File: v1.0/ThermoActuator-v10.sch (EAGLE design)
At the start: 58 parts, among them IC1 LM358D, IC2 ULN2003AD, IC3 LM358D

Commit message: all channels laid out
somewhat inconsistent but all elements
laid out except the button
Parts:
- added C5, C6, C7, C8: 10nF, rcl:C-EUC1206
- added IC4, IC5: LM358D, linear:LM358D
- added JP1: (no value), SparkFun:M06LOCK
- added JP24, JP25, JP26: M022.54MM_SCREWTERM, SparkFun-Connectors:M022.54MM_SCREWTERM
- added R19, R20, R21, R22: 100K, rcl:R-EU_R0805
- added R23, R24, R25, R26: 10K, rcl:R-EU_R1206
- IC1: value LM358D -> ULN2003AD; device linear:LM358D -> uln-udn:ULN2003AD
- IC2: value ULN2003AD -> LM358D; device uln-udn:ULN2003AD -> linear:LM358D
- JP10: value (none) -> M022.54MM_SCREWTERM; device SparkFun:M06LOCK -> SparkFun-Connectors:M022.54MM_SCREWTERM
- JP11, JP12: value (none) -> M022.54MM_SCREWTERM; device SparkFun:M02LOCK -> SparkFun-Connectors:M022.54MM_SCREWTERM
- JP13, JP19, JP20, JP21, JP22, JP23: value ADC2 -> M022.54MM_SCREWTERM
- JP14: value OUT1 -> M022.54MM_SCREWTERM
- JP15: value OUT2 -> (none); device SparkFun-Connectors:M022.54MM_SCREWTERM -> SparkFun:M02LOCK
- JP16, JP17: value ADC2 -> M16LOCK; device SparkFun-Connectors:M022.54MM_SCREWTERM -> SparkFun:M16LOCK
- JP18: value ADC2 -> (none); device SparkFun-Connectors:M022.54MM_SCREWTERM -> SparkFun:M02LOCK
- JP2: value ADC1 -> (none); device SparkFun-Connectors:M022.54MM_SCREWTERM -> SparkFun:M08LOCK
- JP7: value (none) -> M022.54MM_SCREWTERM; device SparkFun:M08LOCK -> SparkFun-Connectors:M022.54MM_SCREWTERM
- JP8, JP9: value M16LOCK -> M022.54MM_SCREWTERM; device SparkFun:M16LOCK -> SparkFun-Connectors:M022.54MM_SCREWTERM
- R1: value 330 -> (none)
- R11, R12, R13, R14: value 330 -> 100K
- R15, R17: value 100K -> 10K; device rcl:R-EU_R0805 -> rcl:R-EU_R1206
- R3: value (none) -> 330
- R4, R6: value 100K -> 330
- R5, R7: value 10K -> 330; device rcl:R-EU_R1206 -> rcl:R-EU_R0805
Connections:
- new net AS4: IC4A.-IN, IC4A.OUT, SW1.12
- new net AS5: IC4B.-IN, IC4B.OUT, SW1.11
- new net AS6: IC5A.-IN, IC5A.OUT, SW1.10
- new net AS7: IC5B.-IN, IC5B.OUT, SW1.9
- new net N$24: JP23.2, R19.1, R23.1
- new net N$25: C5.2, IC4A.+IN, R23.2
- new net N$26: JP24.2, R20.1, R24.1
- new net N$27: C6.2, IC4B.+IN, R24.2
- new net N$28: JP25.2, R21.1, R25.1
- new net N$29: C7.2, IC5A.+IN, R25.2
- new net N$30: JP26.2, R22.1, R26.1
- new net N$31: C8.2, IC5B.+IN, R26.2
- net 3.3: now also JP1.2; no longer JP10.2
- net 5V: now also JP1.3, R2.2; no longer JP10.3, R3.2
- net A10: now also IC1.I3; no longer IC2.I3
- net A11: now also IC1.I4; no longer IC2.I4
- net A12: now also IC1.I5; no longer IC2.I5
- net A13: now also IC1.I6; no longer IC2.I6
- net A14: now also IC1.I7; no longer IC2.I7
- net A8: now also IC1.I1; no longer IC2.I1
- net A9: now also IC1.I2; no longer IC2.I2
- net AO0: now also IC1.O1, JP7.2; no longer IC2.O1, JP14.2
- net AO1: now also IC1.O2, JP8.2; no longer IC2.O2, JP15.2
- net AO2: now also IC1.O3, JP9.2; no longer IC2.O3, JP16.2
- net AO3: now also IC1.O4, JP10.2; no longer IC2.O4, JP17.2
- net AO4: now also IC1.O5, JP11.2; no longer IC2.O5, JP18.2
- net AO5: now also IC1.O6, JP12.2; no longer IC2.O6, JP19.2
- net AO6: now also IC1.O7, JP13.2; no longer IC2.O7, JP20.2
- net AO7: now also JP14.2; no longer JP21.2
- net AREF: now also JP2.8; no longer JP3.8
- net AS0: now also IC2A.-IN, IC2A.OUT; no longer IC1A.-IN, IC1A.OUT
- net AS1: now also IC2B.-IN, IC2B.OUT; no longer IC1B.-IN, IC1B.OUT
- net D10: now also JP2.3; no longer JP3.3
- net D11: now also JP2.4; no longer JP3.4
- net D12: now also JP2.5; no longer JP3.5
- net D13: now also JP2.6, R3.2; no longer JP3.6, R2.2
- net D22: now also JP17.1; no longer JP9.1
- net D23: now also JP16.16; no longer JP8.16
- net D24: now also JP17.2; no longer JP9.2
- net D25: now also JP16.15; no longer JP8.15
- net D26: now also JP17.3; no longer JP9.3
- net D27: now also JP16.14; no longer JP8.14
- net D28: now also JP17.4; no longer JP9.4
- net D29: now also JP16.13; no longer JP8.13
- net D30: now also JP17.5; no longer JP9.5
- net D31: now also JP16.12; no longer JP8.12
- net D32: now also JP17.6; no longer JP9.6
- net D33: now also JP16.11; no longer JP8.11
- net D34: now also JP17.7; no longer JP9.7
- net D35: now also JP16.10; no longer JP8.10
- net D36: now also JP17.8; no longer JP9.8
- net D37: now also JP16.9; no longer JP8.9
- net D38: now also JP17.9; no longer JP9.9
- net D39: now also JP16.8; no longer JP8.8
- net D40: now also JP17.10; no longer JP9.10
- net D41: now also JP16.7; no longer JP8.7
- net D42: now also JP17.11; no longer JP9.11
- net D43: now also JP16.6; no longer JP8.6
- net D44: now also JP17.12; no longer JP9.12
- net D45: now also JP16.5; no longer JP8.5
- net D46: now also JP17.13; no longer JP9.13
- net D47: now also JP16.4; no longer JP8.4
- net D48: now also JP17.14; no longer JP9.14
- net D49: now also JP16.3; no longer JP8.3
- net D50: now also JP17.15; no longer JP9.15
- net D51: now also JP16.2; no longer JP8.2
- net D52: now also JP17.16; no longer JP9.16
- net D53: now also JP16.1; no longer JP8.1
- net D8: now also JP2.1; no longer JP3.1
- net D9: now also JP2.2; no longer JP3.2
- net GND: now also C5.1, C6.1, C7.1, C8.1, IC1.GND, IC2P.V-, IC4P.V-, IC5P.V-, JP1.4, JP1.5, JP14.1, JP18.1, JP18.2, JP19.1, JP2.7, JP20.1, JP24.1, JP25.1, JP26.1; no longer IC1P.V-, IC2.GND, JP10.4, JP10.5, JP11.1, JP11.2, JP13.1, JP2.1, JP3.7
- net N$1: now also JP19.2, R11.1, R15.1; no longer JP2.2, R4.1, R5.1
- net N$10: now also JP3.8; no longer JP7.8
- net N$11: now also JP20.2, R12.1, R16.1; no longer JP13.2, R6.1, R7.1
- net N$12: now also IC2B.+IN, R16.2; no longer IC1B.+IN, R7.2
- net N$126: now also R2.1; no longer R1.1
- net N$127: now also R3.1; no longer R2.1
- net N$13: now also R4.1; no longer R8.1
- net N$14: now also R5.1; no longer R9.1
- net N$15: now also R6.1; no longer R10.1
- net N$16: now also R7.1; no longer R11.1
- net N$17: now also R8.1; no longer R12.1
- net N$18: now also R9.1; no longer R13.1
- net N$19: now also R10.1; no longer R14.1
- net N$2: now also IC2A.+IN, R15.2; no longer IC1A.+IN, R5.2
- net N$20: now also JP21.2, R13.1, R17.1; no longer JP22.2, R15.1, R16.1
- net N$21: now also R17.2; no longer R16.2
- net N$22: now also JP22.2, R14.1; no longer JP23.2, R17.1
- net N$3: now also JP3.1; no longer JP7.1
- net N$4: now also JP3.2; no longer JP7.2
- net N$5: now also JP3.3; no longer JP7.3
- net N$6: now also JP3.4; no longer JP7.4
- net N$7: now also JP3.5; no longer JP7.5
- net N$8: now also JP3.6; no longer JP7.6
- net N$9: now also JP3.7; no longer JP7.7
- net RES: now also JP1.1, R1.1; no longer JP10.1, R3.1
- net VDD: now also IC1.CD+, IC2P.V+, IC4P.V+, IC5P.V+, JP10.1, JP11.1, JP13.1, JP15.2, JP7.1, JP8.1, JP9.1, R19.2, R20.2, R21.2, R22.2, R5.2, R7.2; no longer IC1P.V+, IC2.CD+, JP12.2, JP14.1, JP16.1, JP17.1, JP18.1, JP19.1, JP20.1, R15.2, R17.2
- net VIN: now also JP1.6; no longer JP10.6
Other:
- moved on the sheet: C1, C2, C3, C4, IC3A, IC3B, JP11, JP12, JP13, JP14, JP15, JP18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

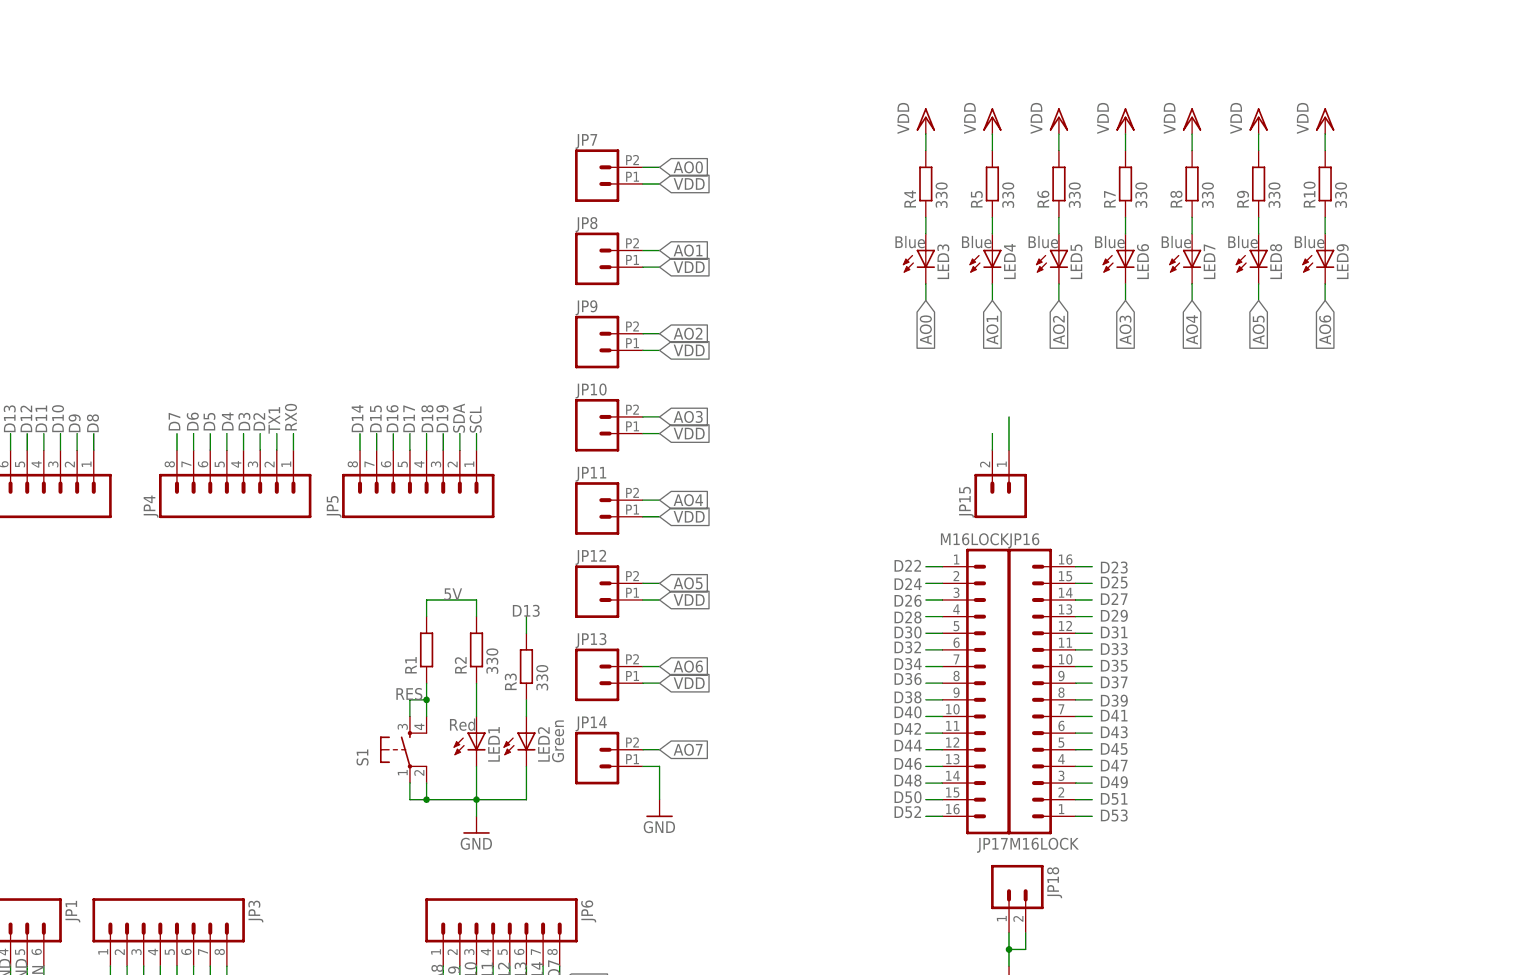
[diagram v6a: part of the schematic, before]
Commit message: local autorouting, no ripup *
almost done. Removed the reset button. Will not be used
on this shield (a higher shield will have it). Laying out
VDD route. Only local auto-route from now on
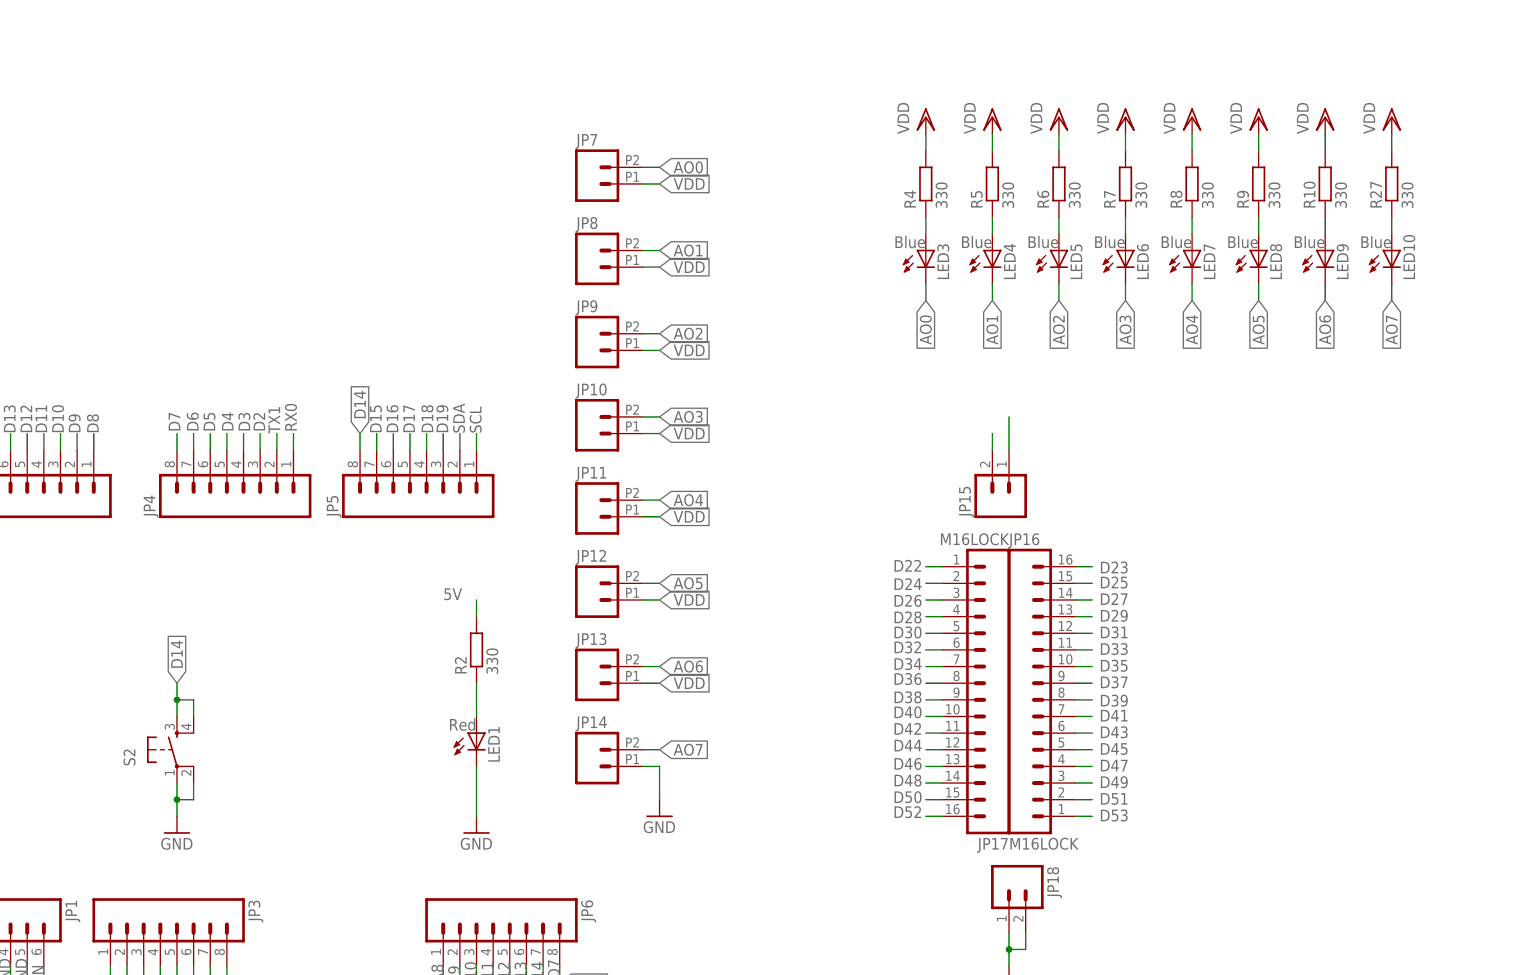
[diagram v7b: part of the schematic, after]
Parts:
- removed LED2: Green, led:LEDCHIP-LED0805
- removed R1: (no value), rcl:R-EU_R0805
- removed R3: 330, rcl:R-EU_R0805
- removed S1: (no value), SparkFun:TAC_SWITCHPTH
- added LED10: Blue, led:LEDCHIP-LED0805
- added R27: 330, rcl:R-EU_R0805
- added S2: (no value), SparkFun:TAC_SWITCHPTH
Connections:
- removed net N$127: LED2.A, R3.1
- new net N$32: LED10.A, R27.1
- net 5V: no longer R1.2
- net AO7: now also LED10.C
- net D13: no longer R3.2
- net D14: now also S2.3, S2.4
- net GND: now also S2.1, S2.2; no longer LED2.C, S1.1, S1.2
- net RES: no longer R1.1, S1.3, S1.4
- net VDD: now also R27.2
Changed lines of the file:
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@@
 <part name="JP18" library="SparkFun" deviceset="M02" device="LOCK"/>
 <part name="JP15" library="SparkFun" deviceset="M02" device="LOCK"/>
-<part name="S1" library="SparkFun" deviceset="TAC_SWITCH" device="PTH"/>
 <part name="LED1" library="led" deviceset="LED" device="CHIP-LED0805" value="Red"/>
-<part name="LED2" library="led" deviceset="LED" device="CHIP-LED0805" value="Green"/>
 <part name="R2" library="rcl" deviceset="R-EU_" device="R0805" value="330"/>
-<part name="R3" library="rcl" deviceset="R-EU_" device="R0805" value="330"/>
-<part name="R1" library="rcl" deviceset="R-EU_" device="R0805"/>
 <part name="GND1" library="SparkFun" deviceset="GND" device=""/>
 <part name="GND4" library="SparkFun" deviceset="GND" device=""/>
@@
 <part name="GND23" library="supply1" deviceset="GND" device=""/>
 <part name="JP26" library="SparkFun-Connectors" deviceset="M02" device="2.54MM_SCREWTERM" value=""/>
+<part name="S2" library="SparkFun" deviceset="TAC_SWITCH" device="PTH"/>
+<part name="GND26" library="SparkFun" deviceset="GND" device=""/>
+<part name="LED10" library="led" deviceset="LED" device="CHIP-LED0805" value="Blue"/>
+<part name="R27" library="rcl" deviceset="R-EU_" device="R0805" value="330"/>
+<part name="VDD20" library="supply1" deviceset="VDD" device=""/>
 </parts>
 <sheets>
@@
 <instance part="JP18" gate="G$1" x="177.8" y="66.04" rot="R270"/>
 <instance part="JP15" gate="G$1" x="177.8" y="124.46" rot="R90"/>
-<instance part="S1" gate="S" x="86.36" y="86.36" rot="R90"/>
 <instance part="LED1" gate="G$1" x="96.52" y="88.9" smashed="yes">
 <attribute name="NAME" x="100.076" y="84.328" size="1.778" layer="95" rot="R90"/>
 <attribute name="VALUE" x="96.52" y="91.059" size="1.778" layer="96" rot="R180"/>
 </instance>
-<instance part="LED2" gate="G$1" x="104.14" y="88.9" smashed="yes">
-<attribute name="NAME" x="107.696" y="84.328" size="1.778" layer="95" rot="R90"/>
-<attribute name="VALUE" x="109.855" y="84.328" size="1.778" layer="96" rot="R90"/>
-</instance>
 <instance part="R2" gate="G$1" x="96.52" y="101.6" rot="R90"/>
-<instance part="R3" gate="G$1" x="104.14" y="99.06" rot="R90"/>
-<instance part="R1" gate="G$1" x="88.9" y="101.6" rot="R90"/>
 <instance part="GND1" gate="1" x="96.52" y="73.66"/>
 <instance part="GND4" gate="1" x="177.8" y="50.8"/>
@@
 <instance part="GND23" gate="1" x="416.56" y="7.62"/>
 <instance part="JP26" gate="G$1" x="378.46" y="20.32"/>
+<instance part="S2" gate="S" x="50.8" y="86.36" rot="R90"/>
+<instance part="GND26" gate="1" x="50.8" y="73.66"/>
+<instance part="LED10" gate="G$1" x="236.22" y="162.56" smashed="yes">
+<attribute name="NAME" x="239.776" y="157.988" size="1.778" layer="95" rot="R90"/>
+<attribute name="VALUE" x="236.22" y="164.719" size="1.778" layer="96" rot="R180"/>
+</instance>
+<instance part="R27" gate="G$1" x="236.22" y="172.72" rot="R90"/>
+<instance part="VDD20" gate="G$1" x="236.22" y="182.88"/>
 </instances>
 <busses>
@@
 <pinref part="JP1" gate="G$1" pin="1"/>
 </segment>
-<segment>
-<wire x1="88.9" y1="96.52" x2="88.9" y2="93.98" width="0.1524" layer="91"/>
-<wire x1="88.9" y1="93.98" x2="88.9" y2="91.44" width="0.1524" layer="91"/>
-<wire x1="86.36" y1="91.44" x2="86.36" y2="93.98" width="0.1524" layer="91"/>
-<wire x1="86.36" y1="93.98" x2="88.9" y2="93.98" width="0.1524" layer="91"/>
-<junction x="88.9" y="93.98"/>
-<label x="84.074" y="93.98" size="1.778" layer="95"/>
-<pinref part="R1" gate="G$1" pin="1"/>
-<pinref part="S1" gate="S" pin="4"/>
-<pinref part="S1" gate="S" pin="3"/>
-</segment>
 </net>
 <net name="3.3" class="0">
@@
 </segment>
 <segment>
-<wire x1="88.9" y1="106.68" x2="88.9" y2="109.22" width="0.1524" layer="91"/>
 <wire x1="96.52" y1="106.68" x2="96.52" y2="109.22" width="0.1524" layer="91"/>
-<wire x1="96.52" y1="109.22" x2="88.9" y2="109.22" width="0.1524" layer="91"/>
 <label x="91.44" y="109.22" size="1.778" layer="95"/>
-<pinref part="R1" gate="G$1" pin="2"/>
 <pinref part="R2" gate="G$1" pin="2"/>
 </segment>
@@
 </segment>
 <segment>
-<wire x1="96.52" y1="76.2" x2="96.52" y2="78.74" width="0.1524" layer="91"/>
-<wire x1="86.36" y1="81.28" x2="86.36" y2="78.74" width="0.1524" layer="91"/>
-<wire x1="86.36" y1="78.74" x2="88.9" y2="78.74" width="0.1524" layer="91"/>
-<wire x1="88.9" y1="78.74" x2="96.52" y2="78.74" width="0.1524" layer="91"/>
-<wire x1="88.9" y1="81.28" x2="88.9" y2="78.74" width="0.1524" layer="91"/>
-<wire x1="96.52" y1="83.82" x2="96.52" y2="78.74" width="0.1524" layer="91"/>
-<wire x1="104.14" y1="83.82" x2="104.14" y2="78.74" width="0.1524" layer="91"/>
-<wire x1="104.14" y1="78.74" x2="96.52" y2="78.74" width="0.1524" layer="91"/>
-<junction x="88.9" y="78.74"/>
-<junction x="96.52" y="78.74"/>
+<wire x1="96.52" y1="83.82" x2="96.52" y2="76.2" width="0.1524" layer="91"/>
 <pinref part="GND1" gate="1" pin="GND"/>
-<pinref part="S1" gate="S" pin="1"/>
-<pinref part="S1" gate="S" pin="2"/>
 <pinref part="LED1" gate="G$1" pin="C"/>
-<pinref part="LED2" gate="G$1" pin="C"/>
 </segment>
 <segment>
@@
 <wire x1="416.56" y1="10.16" x2="416.56" y2="12.7" width="0.1524" layer="91"/>
 </segment>
+<segment>
+<pinref part="S2" gate="S" pin="1"/>
+<pinref part="GND26" gate="1" pin="GND"/>
+<wire x1="50.8" y1="81.28" x2="50.8" y2="78.74" width="0.1524" layer="91"/>
+<pinref part="S2" gate="S" pin="2"/>
+<wire x1="50.8" y1="78.74" x2="50.8" y2="76.2" width="0.1524" layer="91"/>
+<wire x1="53.34" y1="81.28" x2="53.34" y2="78.74" width="0.1524" layer="91"/>
+<wire x1="53.34" y1="78.74" x2="50.8" y2="78.74" width="0.1524" layer="91"/>
+<junction x="50.8" y="78.74"/>
+</segment>
 </net>
 <net name="VIN" class="0">
@@
 <pinref part="JP2" gate="G$1" pin="6"/>
 </segment>
-<segment>
-<wire x1="104.14" y1="104.14" x2="104.14" y2="106.68" width="0.1524" layer="91"/>
-<label x="101.854" y="106.68" size="1.778" layer="95"/>
-<pinref part="R3" gate="G$1" pin="2"/>
-</segment>
 </net>
 <net name="AREF" class="0">
@@
 <net name="D14" class="0">
 <segment>
-<wire x1="78.74" y1="134.62" x2="78.74" y2="132.08" width="0.1524" layer="91"/>
-<label x="79.248" y="134.62" size="1.778" layer="95" rot="R90"/>
 <pinref part="JP5" gate="G$1" pin="8"/>
+<wire x1="78.74" y1="132.08" x2="78.74" y2="134.62" width="0.1524" layer="91"/>
+<label x="78.74" y="134.62" size="1.778" layer="95" rot="R90" xref="yes"/>
+</segment>
+<segment>
+<pinref part="S2" gate="S" pin="3"/>
+<wire x1="50.8" y1="91.44" x2="50.8" y2="93.98" width="0.1524" layer="91"/>
+<pinref part="S2" gate="S" pin="4"/>
+<wire x1="53.34" y1="91.44" x2="53.34" y2="93.98" width="0.1524" layer="91"/>
+<wire x1="53.34" y1="93.98" x2="50.8" y2="93.98" width="0.1524" layer="91"/>
+<wire x1="50.8" y1="93.98" x2="50.8" y2="96.52" width="0.1524" layer="91"/>
+<junction x="50.8" y="93.98"/>
+<label x="50.8" y="96.52" size="1.778" layer="95" rot="R90" xref="yes"/>
 </segment>
 </net>
@@
 <pinref part="R2" gate="G$1" pin="1"/>
 <pinref part="LED1" gate="G$1" pin="A"/>
-</segment>
-</net>
-<net name="N$127" class="0">
-<segment>
-<wire x1="104.14" y1="93.98" x2="104.14" y2="91.44" width="0.1524" layer="91"/>
-<pinref part="R3" gate="G$1" pin="1"/>
-<pinref part="LED2" gate="G$1" pin="A"/>
 </segment>
 </net>
@@
 <pinref part="VDD17" gate="G$1" pin="VDD"/>
 <wire x1="398.78" y1="35.56" x2="398.78" y2="38.1" width="0.1524" layer="91"/>
+</segment>
+<segment>
+<pinref part="VDD20" gate="G$1" pin="VDD"/>
+<pinref part="R27" gate="G$1" pin="2"/>
+<wire x1="236.22" y1="180.34" x2="236.22" y2="177.8" width="0.1524" layer="91"/>
 </segment>
 </net>
@@
 <label x="124.46" y="86.36" size="1.778" layer="95" xref="yes"/>
 </segment>
+<segment>
+<pinref part="LED10" gate="G$1" pin="C"/>
+<wire x1="236.22" y1="157.48" x2="236.22" y2="154.94" width="0.1524" layer="91"/>
+<label x="236.22" y="154.94" size="1.778" layer="95" rot="R270" xref="yes"/>
+</segment>
 </net>
 <net name="N$13" class="0">
@@
 </segment>
 </net>
+<net name="N$32" class="0">
+<segment>
+<pinref part="R27" gate="G$1" pin="1"/>
+<pinref part="LED10" gate="G$1" pin="A"/>
+<wire x1="236.22" y1="167.64" x2="236.22" y2="165.1" width="0.1524" layer="91"/>
+</segment>
+</net>
